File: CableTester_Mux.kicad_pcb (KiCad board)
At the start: 2 copper layers, 30.5 x 63.5 mm, 10 parts, among them J1 7-188275-8, J2 7-188275-8, J3 7-188275-8, J4 7-188275-8, J5 1787072, J6 Signal, J7 Conn_01x04_MountingPin, J8 Conn_01x04_MountingPin, U1 DG1206EUI+

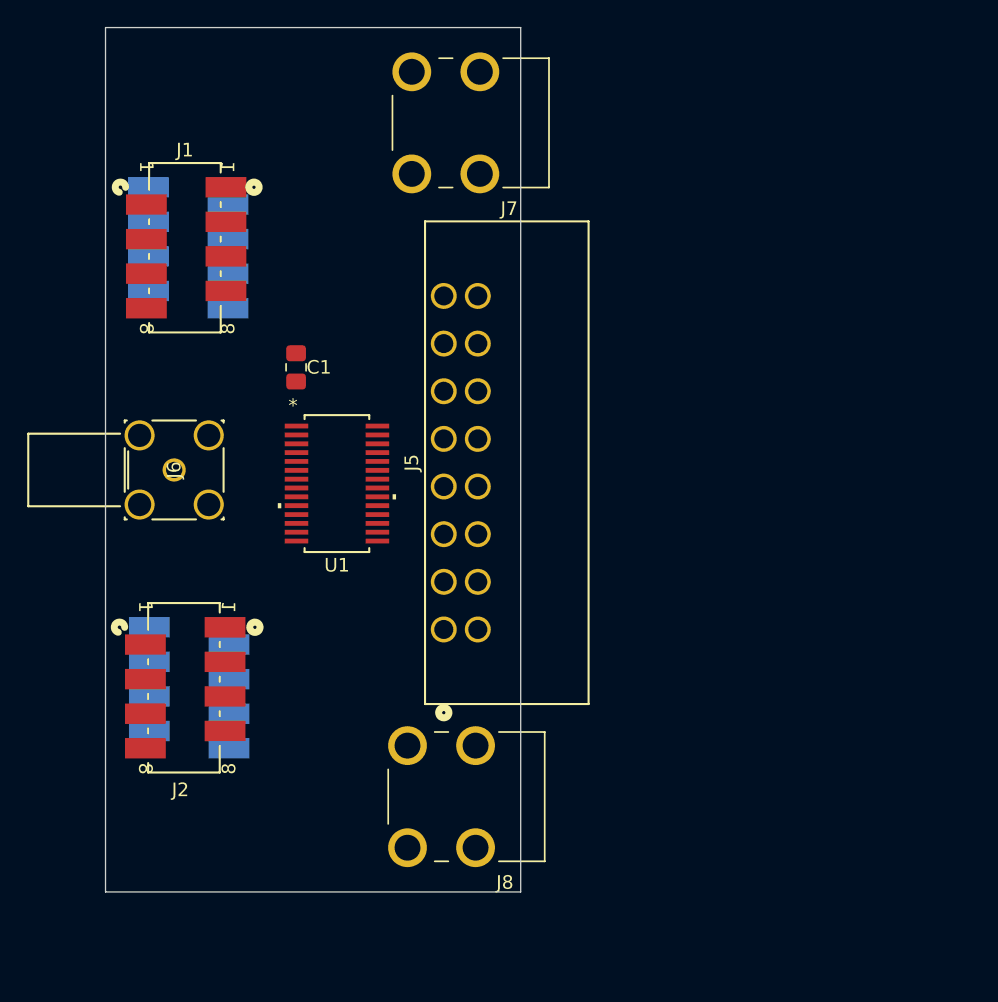
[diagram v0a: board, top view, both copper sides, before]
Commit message: Fixed/Completed Initial Libraries
-Completed initial libraries
-Updated schematic and layout with part metadata
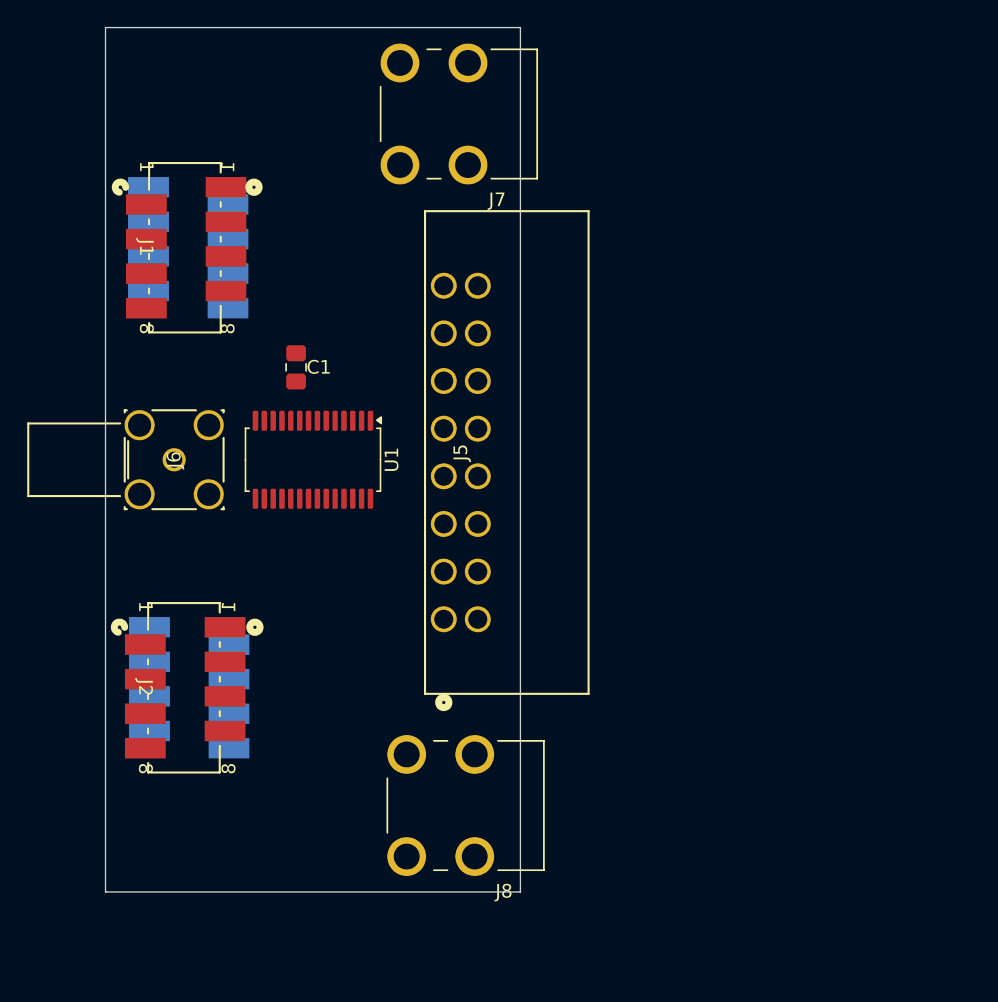
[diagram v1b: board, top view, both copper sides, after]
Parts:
- J1, J2, J3, J4: value 7-188275-8 -> MircoMatch; footprint footprints:CONN_7-188275-8_TYC -> Footprints:CONN_7-188275-8_TYC
- J5: footprint footprints:CONN_1787072_PXC -> Footprints:CONN_1787072_PXC
- J6: value Signal -> SMB; footprint footprints:CONN_142146_AMP -> Footprints:CONN_142146_AMP
- J7, J8: value Conn_01x04_MountingPin -> Keystone 7792; footprint footprints:KEYSTONE_7792 -> Footprints:KEYSTONE_7792
- U1: footprint footprints:21-0066O_U28&plus_2_MXM-M -> Package_SO:TSSOP-28_4.4x9.7mm_P0.65mm
- moved U1 2.48 mm to (145.2, 93.2), turned to -90 degrees
- moved J7 1.09 mm to (154.1, 67.8)
- moved J5 0.75 mm to (154.8, 104.9)
- moved J6 0.75 mm to (135.0, 93.2)
- moved J8 0.65 mm to (154.6, 118.6)

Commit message: updated lib links and metadata
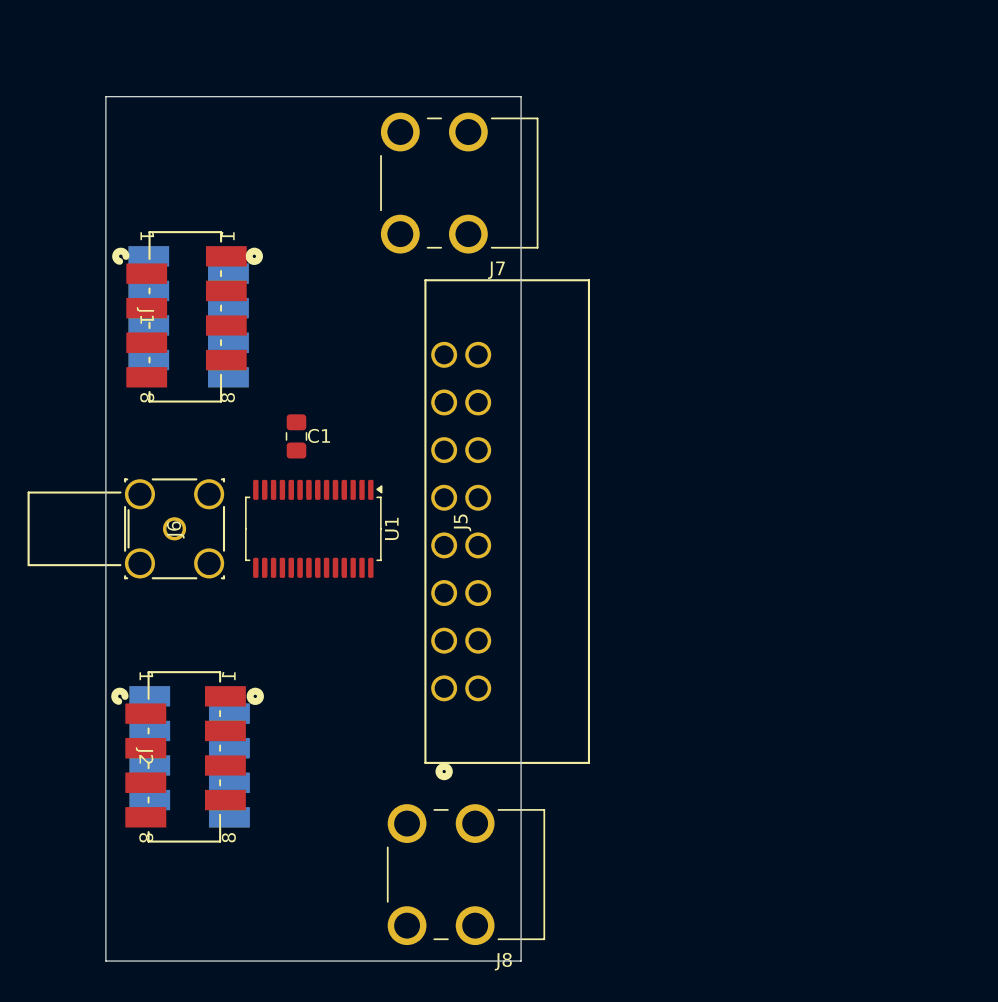
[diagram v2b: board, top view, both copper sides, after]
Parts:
- moved C1 5.08 mm to (144.0, 91.5)
- moved J1 5.08 mm to (133.0, 78.2)
- moved J2 5.08 mm to (132.9, 110.6)
- moved J3 5.08 mm to (139.0, 78.2)
- moved J4 5.08 mm to (139.1, 110.6)
- moved J5 5.08 mm to (154.8, 110.0)
- moved J6 5.08 mm to (135.0, 98.2)
- moved J8 5.08 mm to (154.6, 123.7)
- moved U1 5.08 mm to (145.2, 98.2)
- moved J7 5.08 mm to (154.1, 72.8)
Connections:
- J6 pad 3: (no net) -> GND
- J6 pad 4: (no net) -> GND
- J6 pad 5: (no net) -> GND

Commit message: Updated Schematics with filter for AC UART signaling
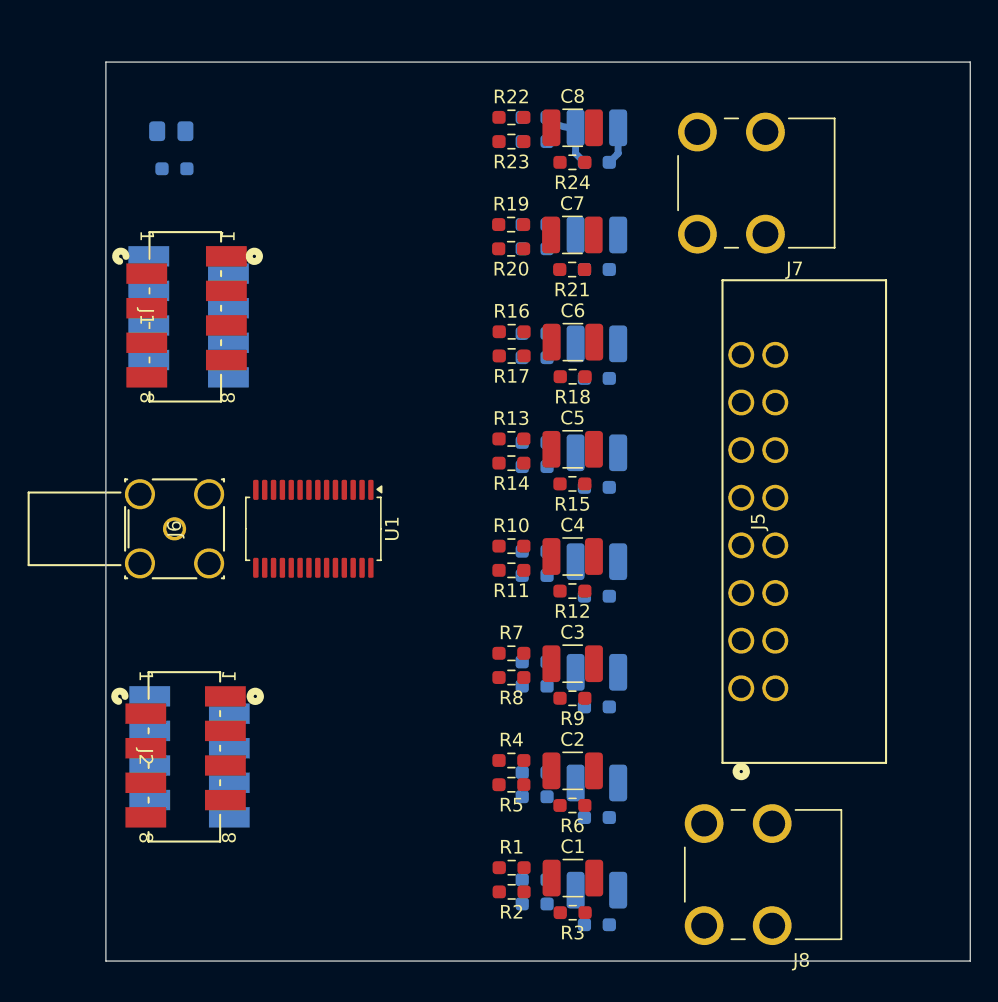
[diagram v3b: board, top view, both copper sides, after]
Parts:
- added C10: 10uF, Capacitor_SMD:C_1210_3225Metric_Pad1.33x2.70mm_HandSolder, B.Cu at (166.1, 116.9)
- added C100: 100nF, Capacitor_SMD:C_0805_2012Metric_Pad1.18x1.45mm_HandSolder, B.Cu at (134.8, 69.0)
- added C11: 10uF, Capacitor_SMD:C_1210_3225Metric_Pad1.33x2.70mm_HandSolder, B.Cu at (166.1, 108.8)
- added C12: 10uF, Capacitor_SMD:C_1210_3225Metric_Pad1.33x2.70mm_HandSolder, B.Cu at (166.1, 100.7)
- added C13: 10uF, Capacitor_SMD:C_1210_3225Metric_Pad1.33x2.70mm_HandSolder, B.Cu at (166.1, 92.7)
- added C14: 10uF, Capacitor_SMD:C_1210_3225Metric_Pad1.33x2.70mm_HandSolder, B.Cu at (166.1, 84.7)
- added C15: 10uF, Capacitor_SMD:C_1210_3225Metric_Pad1.33x2.70mm_HandSolder, B.Cu at (166.1, 76.7)
- added C16: 10uF, Capacitor_SMD:C_1210_3225Metric_Pad1.33x2.70mm_HandSolder, B.Cu at (166.1, 68.8)
- added C2: 10uF, Capacitor_SMD:C_1210_3225Metric_Pad1.33x2.70mm_HandSolder, F.Cu at (164.3, 116.0)
- added C3: 10uF, Capacitor_SMD:C_1210_3225Metric_Pad1.33x2.70mm_HandSolder, F.Cu at (164.3, 108.2)
- added C4: 10uF, Capacitor_SMD:C_1210_3225Metric_Pad1.33x2.70mm_HandSolder, F.Cu at (164.3, 100.3)
- added C5: 10uF, Capacitor_SMD:C_1210_3225Metric_Pad1.33x2.70mm_HandSolder, F.Cu at (164.3, 92.4)
- added C6: 10uF, Capacitor_SMD:C_1210_3225Metric_Pad1.33x2.70mm_HandSolder, F.Cu at (164.3, 84.5)
- added C7: 10uF, Capacitor_SMD:C_1210_3225Metric_Pad1.33x2.70mm_HandSolder, F.Cu at (164.3, 76.7)
- added C8: 10uF, Capacitor_SMD:C_1210_3225Metric_Pad1.33x2.70mm_HandSolder, F.Cu at (164.3, 68.8)
- added C9: 10uF, Capacitor_SMD:C_1210_3225Metric_Pad1.33x2.70mm_HandSolder, B.Cu at (166.1, 124.8)
- added R1: 100k, Resistor_SMD:R_0603_1608Metric_Pad0.98x0.95mm_HandSolder, F.Cu at (159.8, 123.1)
- added R10: 100k, Resistor_SMD:R_0603_1608Metric_Pad0.98x0.95mm_HandSolder, F.Cu at (159.8, 99.5)
- added R11: 100k, Resistor_SMD:R_0603_1608Metric_Pad0.98x0.95mm_HandSolder, F.Cu at (159.8, 101.3)
- added R12: 0R, Resistor_SMD:R_0603_1608Metric_Pad0.98x0.95mm_HandSolder, F.Cu at (164.3, 102.8)
- added R13: 100k, Resistor_SMD:R_0603_1608Metric_Pad0.98x0.95mm_HandSolder, F.Cu at (159.8, 91.6)
- added R14: 100k, Resistor_SMD:R_0603_1608Metric_Pad0.98x0.95mm_HandSolder, F.Cu at (159.8, 93.4)
- added R15: 0R, Resistor_SMD:R_0603_1608Metric_Pad0.98x0.95mm_HandSolder, F.Cu at (164.3, 94.9)
- added R16: 100k, Resistor_SMD:R_0603_1608Metric_Pad0.98x0.95mm_HandSolder, F.Cu at (159.8, 83.8)
- added R17: 100k, Resistor_SMD:R_0603_1608Metric_Pad0.98x0.95mm_HandSolder, F.Cu at (159.8, 85.5)
- added R18: 0R, Resistor_SMD:R_0603_1608Metric_Pad0.98x0.95mm_HandSolder, F.Cu at (164.3, 87.1)
- added R19: 100k, Resistor_SMD:R_0603_1608Metric_Pad0.98x0.95mm_HandSolder, F.Cu at (159.8, 75.9)
- added R2: 100k, Resistor_SMD:R_0603_1608Metric_Pad0.98x0.95mm_HandSolder, F.Cu at (159.8, 124.9)
- added R20: 100k, Resistor_SMD:R_0603_1608Metric_Pad0.98x0.95mm_HandSolder, F.Cu at (159.8, 77.7)
- added R21: 0R, Resistor_SMD:R_0603_1608Metric_Pad0.98x0.95mm_HandSolder, F.Cu at (164.3, 79.2)
- added R22: 100k, Resistor_SMD:R_0603_1608Metric_Pad0.98x0.95mm_HandSolder, F.Cu at (159.8, 68.0)
- added R23: 100k, Resistor_SMD:R_0603_1608Metric_Pad0.98x0.95mm_HandSolder, F.Cu at (159.8, 69.8)
- added R24: 0R, Resistor_SMD:R_0603_1608Metric_Pad0.98x0.95mm_HandSolder, F.Cu at (164.3, 71.3)
- added R25: 100k, Resistor_SMD:R_0603_1608Metric_Pad0.98x0.95mm_HandSolder, B.Cu at (161.5, 124.0)
- added R26: 100k, Resistor_SMD:R_0603_1608Metric_Pad0.98x0.95mm_HandSolder, B.Cu at (161.5, 125.8)
- added R27: 0R, Resistor_SMD:R_0603_1608Metric_Pad0.98x0.95mm_HandSolder, B.Cu at (166.1, 127.3)
- added R28: 100k, Resistor_SMD:R_0603_1608Metric_Pad0.98x0.95mm_HandSolder, B.Cu at (161.5, 116.2)
- added R29: 100k, Resistor_SMD:R_0603_1608Metric_Pad0.98x0.95mm_HandSolder, B.Cu at (161.5, 117.9)
- added R3: 0R, Resistor_SMD:R_0603_1608Metric_Pad0.98x0.95mm_HandSolder, F.Cu at (164.3, 126.4)
- added R30: 0R, Resistor_SMD:R_0603_1608Metric_Pad0.98x0.95mm_HandSolder, B.Cu at (166.1, 119.5)
- added R31: 100k, Resistor_SMD:R_0603_1608Metric_Pad0.98x0.95mm_HandSolder, B.Cu at (161.5, 108.0)
- added R32: 100k, Resistor_SMD:R_0603_1608Metric_Pad0.98x0.95mm_HandSolder, B.Cu at (161.5, 109.8)
- added R33: 0R, Resistor_SMD:R_0603_1608Metric_Pad0.98x0.95mm_HandSolder, B.Cu at (166.1, 111.3)
- added R34: 100k, Resistor_SMD:R_0603_1608Metric_Pad0.98x0.95mm_HandSolder, B.Cu at (161.5, 99.9)
- added R35: 100k, Resistor_SMD:R_0603_1608Metric_Pad0.98x0.95mm_HandSolder, B.Cu at (161.5, 101.7)
- added R36: 0R, Resistor_SMD:R_0603_1608Metric_Pad0.98x0.95mm_HandSolder, B.Cu at (166.1, 103.2)
- added R37: 100k, Resistor_SMD:R_0603_1608Metric_Pad0.98x0.95mm_HandSolder, B.Cu at (161.5, 91.9)
- added R38: 100k, Resistor_SMD:R_0603_1608Metric_Pad0.98x0.95mm_HandSolder, B.Cu at (161.5, 93.7)
- added R39: 0R, Resistor_SMD:R_0603_1608Metric_Pad0.98x0.95mm_HandSolder, B.Cu at (166.1, 95.2)
- added R4: 100k, Resistor_SMD:R_0603_1608Metric_Pad0.98x0.95mm_HandSolder, F.Cu at (159.8, 115.3)
- added R40: 100k, Resistor_SMD:R_0603_1608Metric_Pad0.98x0.95mm_HandSolder, B.Cu at (161.5, 83.9)
- added R41: 100k, Resistor_SMD:R_0603_1608Metric_Pad0.98x0.95mm_HandSolder, B.Cu at (161.5, 85.7)
- added R42: 0R, Resistor_SMD:R_0603_1608Metric_Pad0.98x0.95mm_HandSolder, B.Cu at (166.1, 87.2)
- added R43: 100k, Resistor_SMD:R_0603_1608Metric_Pad0.98x0.95mm_HandSolder, B.Cu at (161.5, 75.9)
- added R44: 100k, Resistor_SMD:R_0603_1608Metric_Pad0.98x0.95mm_HandSolder, B.Cu at (161.5, 77.7)
- added R45: 0R, Resistor_SMD:R_0603_1608Metric_Pad0.98x0.95mm_HandSolder, B.Cu at (166.1, 79.2)
- added R46: 100k, Resistor_SMD:R_0603_1608Metric_Pad0.98x0.95mm_HandSolder, B.Cu at (161.5, 68.0)
- added R47: 100k, Resistor_SMD:R_0603_1608Metric_Pad0.98x0.95mm_HandSolder, B.Cu at (161.5, 69.8)
- added R48: 0R, Resistor_SMD:R_0603_1608Metric_Pad0.98x0.95mm_HandSolder, B.Cu at (166.1, 71.3)
- added R49: 0R, Resistor_SMD:R_0603_1608Metric_Pad0.98x0.95mm_HandSolder, B.Cu at (135.0, 71.8)
- added R5: 100k, Resistor_SMD:R_0603_1608Metric_Pad0.98x0.95mm_HandSolder, F.Cu at (159.8, 117.0)
- added R6: 0R, Resistor_SMD:R_0603_1608Metric_Pad0.98x0.95mm_HandSolder, F.Cu at (164.3, 118.6)
- added R7: 100k, Resistor_SMD:R_0603_1608Metric_Pad0.98x0.95mm_HandSolder, F.Cu at (159.8, 107.4)
- added R8: 100k, Resistor_SMD:R_0603_1608Metric_Pad0.98x0.95mm_HandSolder, F.Cu at (159.8, 109.2)
- added R9: 0R, Resistor_SMD:R_0603_1608Metric_Pad0.98x0.95mm_HandSolder, F.Cu at (164.3, 110.7)
- C1: value 100nF -> 10uF; footprint Capacitor_SMD:C_0805_2012Metric_Pad1.18x1.45mm_HandSolder -> Capacitor_SMD:C_1210_3225Metric_Pad1.33x2.70mm_HandSolder
- moved C1 38.3 mm to (164.3, 123.9), turned to 0 degrees
- moved J5 21.8 mm to (176.7, 110.0)
- moved J7 21.8 mm to (176.0, 72.8)
- moved J8 21.8 mm to (176.4, 123.7)
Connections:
- C1 pad 1: +5V -> /Mux1
- C1 pad 2: Net-(U1-VPOS) -> /Jack1
- J1 pad 2: +5V -> +3.3V
- J2 pad 2: +5V -> +3.3V
- J3 pad 2: +5V -> +3.3V
- J4 pad 2: +5V -> +3.3V
- J5 pad 1: /Mux1 -> /Jack1
- J5 pad 10: /Mux10 -> /Jack10
- J5 pad 11: /Mux11 -> /Jack11
- J5 pad 12: /Mux12 -> /Jack12
- J5 pad 13: /Mux13 -> /Jack13
- J5 pad 14: /Mux14 -> /Jack14
- J5 pad 15: /Mux15 -> /Jack15
- J5 pad 16: /Mux16 -> /Jack16
- J5 pad 2: /Mux2 -> /Jack2
- J5 pad 3: /Mux3 -> /Jack3
- J5 pad 4: /Mux4 -> /Jack4
- J5 pad 5: /Mux5 -> /Jack5
- J5 pad 6: /Mux6 -> /Jack6
- J5 pad 7: /Mux7 -> /Jack7
- J5 pad 8: /Mux8 -> /Jack8
- J5 pad 9: /Mux9 -> /Jack9
- U1 pad 1: Net-(U1-VPOS) -> +5V
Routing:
- net /Mux16: track 0.00 -> 6.87 mm
- net /Jack16: track 0.00 -> 2.81 mm
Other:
- board size 30.5 x 63.5 mm -> 63.5 x 66 mm

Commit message: Updated Layout and added 3dmodel
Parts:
- C100, R49: moved to F.Cu
- moved C100 23.5 mm to (146.5, 89.4)
- moved R49 19.5 mm to (154.1, 67.8), turned to 0 degrees
- moved U1 2.84 mm to (147.8, 97.0), turned to 0 degrees
- moved J1 2.34 mm to (133.8, 76.0)
- moved J3 2.21 mm to (138.9, 76.0)
- moved J2 1.73 mm to (133.8, 109.0)
- moved J4 1.52 mm to (138.9, 109.0)
- moved J6 1.27 mm to (135.1, 97.0)
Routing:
- net +5V: track 0.00 -> 47.0 mm
- net /A3: track 0.00 -> 43.7 mm
- net /A1: track 0.00 -> 42.7 mm
- net /Enable: track 0.00 -> 41.6 mm
- net /A2: track 0.00 -> 37.4 mm
- net /A0: track 0.00 -> 36.3 mm
- net +3.3V: track 0.00 -> 36.2 mm
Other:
- board size 63.5 x 66 mm -> 52.1 x 66 mm
- board text added: "ALS-U Controls Cable Tester Mux Pedro Rodriguez"

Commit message: Updated Routing
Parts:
- moved U1 2.54 mm to (150.3, 97.0)
- moved C100 2.27 mm to (148.5, 90.4)
- moved J1 0.48 mm to (134.3, 76.0)
- moved J2 0.48 mm to (134.3, 109.0)
- moved J3 0.48 mm to (139.4, 76.0)
- moved J4 0.48 mm to (139.4, 109.0)
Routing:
- net /A2: track 37.4 -> 80.3 mm, vias 0 -> 3
- net /A0: track 36.3 -> 78.1 mm, vias 0 -> 3
- net /A1: track 42.7 -> 78.4 mm, vias 0 -> 3
- net /Enable: track 41.6 -> 74.6 mm, vias 0 -> 3
- net Net-(J6-In): track 0.00 -> 27.5 mm
- net /Mux1: track 0.00 -> 25.8 mm
- net /Mux8: track 0.00 -> 25.5 mm
- net /Mux2: track 0.00 -> 21.3 mm
- net /Mux7: track 0.00 -> 20.0 mm
- net /Mux3: track 0.00 -> 14.4 mm
- net /A3: track 43.7 -> 56.8 mm, vias 0 -> 3
- net /Mux6: track 0.00 -> 12.2 mm
- net +5V: track 47.0 -> 59.1 mm, vias 0 -> 2
- net +3.3V: track 36.2 -> 46.5 mm, vias 0 -> 2
- net /Mux4: track 0.00 -> 6.07 mm
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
